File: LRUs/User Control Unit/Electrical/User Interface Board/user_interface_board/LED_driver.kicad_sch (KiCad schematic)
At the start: 1 part, among them U2 LP5012PWR

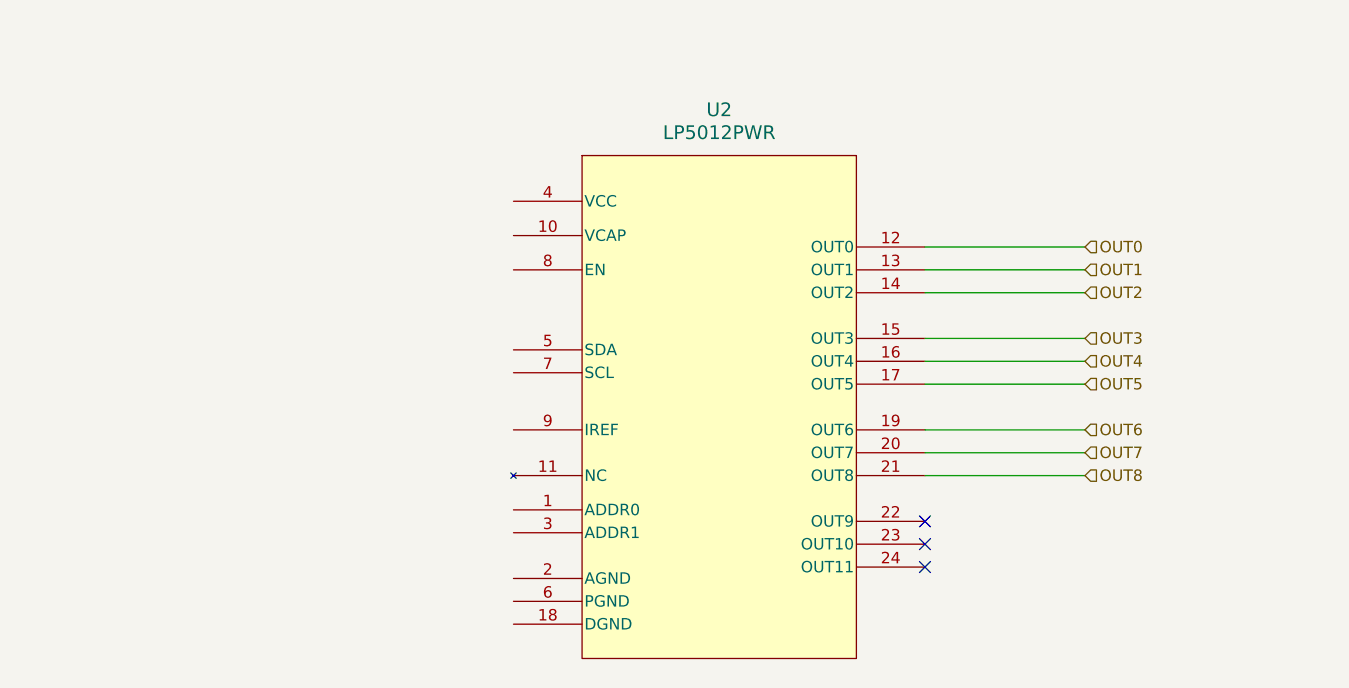
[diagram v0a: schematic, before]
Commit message: interface board schematic
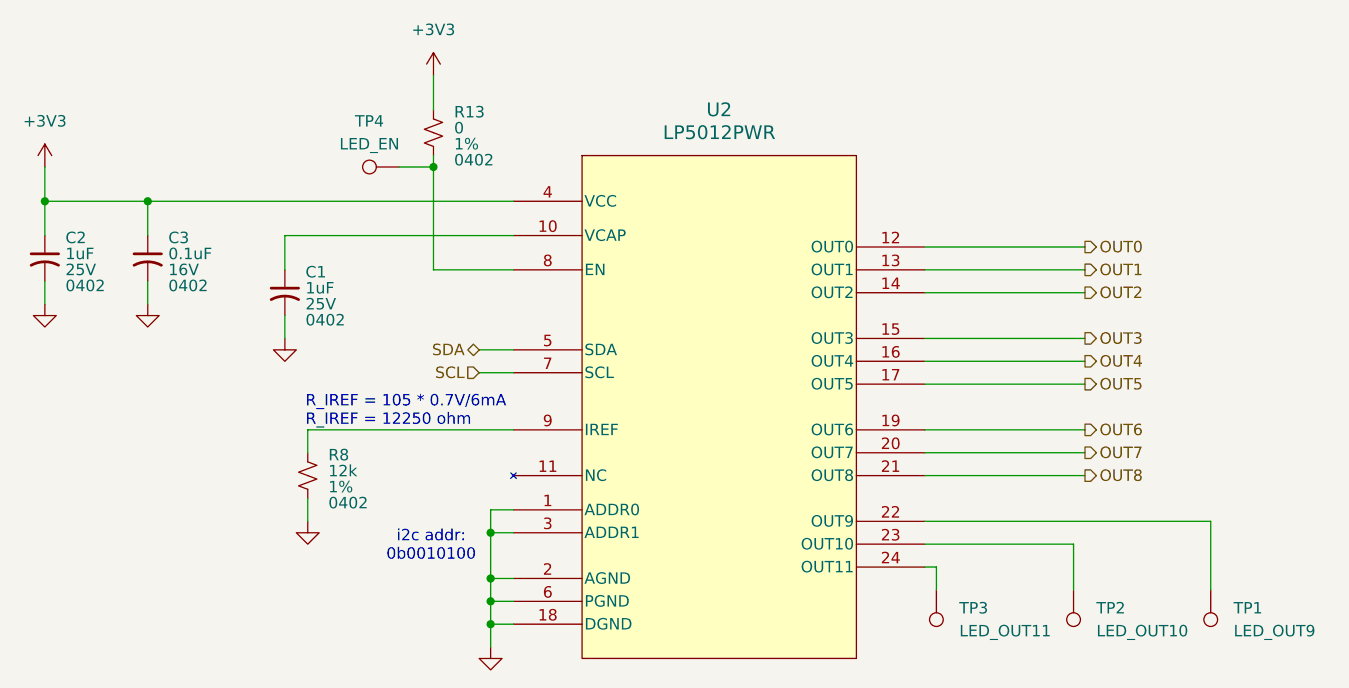
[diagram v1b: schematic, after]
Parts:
- added C1, C2: 1uF, Capacitor_SMD:C_0402_1005Metric, symbol Device:C_Small_US
- added C3: 0.1uF, Capacitor_SMD:C_0402_1005Metric, symbol Device:C_Small_US
- added R13: 0, Resistor_SMD:R_0402_1005Metric, symbol Device:R_Small_US
- added R8: 12k, Resistor_SMD:R_0402_1005Metric, symbol Device:R_Small_US
- added TP1: LED_OUT9, TestPoint:TestPoint_Pad_D1.5mm, symbol Connector:TestPoint
- added TP2: LED_OUT10, TestPoint:TestPoint_Pad_D1.5mm, symbol Connector:TestPoint
- added TP3: LED_OUT11, TestPoint:TestPoint_Pad_D1.5mm, symbol Connector:TestPoint
- added TP4: LED_EN, TestPoint:TestPoint_Pad_D1.5mm, symbol Connector:TestPoint
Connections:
- net GND: now reaches U2.1 (ADDR0)
- net GND: now also U2.18 (DGND), U2.2 (AGND), U2.3 (ADDR1), U2.6 (PGND), C1.2, C2.2, C3.2, R8.2
- net at U2.10 (VCAP): now also C1.1
- net at U2.22 (OUT9): now also TP1.1
- net at U2.23 (OUT10): now also TP2.1
- net at U2.24 (OUT11): now also TP3.1
- net +3V3: now reaches U2.4 (VCC)
- net +3V3: now also C2.1, C3.1, R13.1
- net SDA: now reaches U2.5 (SDA)
- net SCL: now reaches U2.7 (SCL)
- net at U2.8 (EN): now also R13.2, TP4.1
- net at U2.9 (IREF): now also R8.1
- no-connect marks 3 -> 0
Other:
- note added: "R_IREF = 105 * 0.7V/6mA R_IREF = 12250 ohm"
- note added: "i2c addr: 0b0010100"

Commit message: fix drc & add level shifter
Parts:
- U2: footprint footprints:TSSOP_012PWR_TEX -> Project Library:TSSOP_012PWR_TEX; symbol pcb_symbols:LP5012PWR -> Project Library:LP5012PWR
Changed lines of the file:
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@@
 	)
 	(symbol
-		(lib_id "pcb_symbols:LP5012PWR")
+		(lib_id "Project Library:LP5012PWR")
 		(at 124.46 73.66 0)
 		(unit 1)
@@
 			)
 		)
-		(property "Footprint" "footprints:TSSOP_012PWR_TEX"
+		(property "Footprint" "Project Library:TSSOP_012PWR_TEX"
 			(at 146.558 56.134 0)
 			(hide yes)

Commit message: style & add prod files
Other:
- title: (none) -> LED Driver
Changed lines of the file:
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@@
 	(generator_version "10.0")
 	(paper "A4")
+	(title_block
+		(title "LED Driver")
+		(date "2026-10-26")
+		(rev "A")
+	)
 	(text "R_IREF = 105 * 0.7V/6mA\nR_IREF = 12250 ohm"
 		(exclude_from_sim no)
